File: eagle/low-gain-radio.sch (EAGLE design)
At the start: 118 parts, among them U1 MKW01Z128, U2 SKY65116, U3 W25Q80DV, U4 LP5907MFX-3.3, U5 NC7SZ05, U6 LP5907MFX-3.3, U7 LD39200, U8 MAAL-010704, U9 SKY13405-490LF, Y1 32MHz

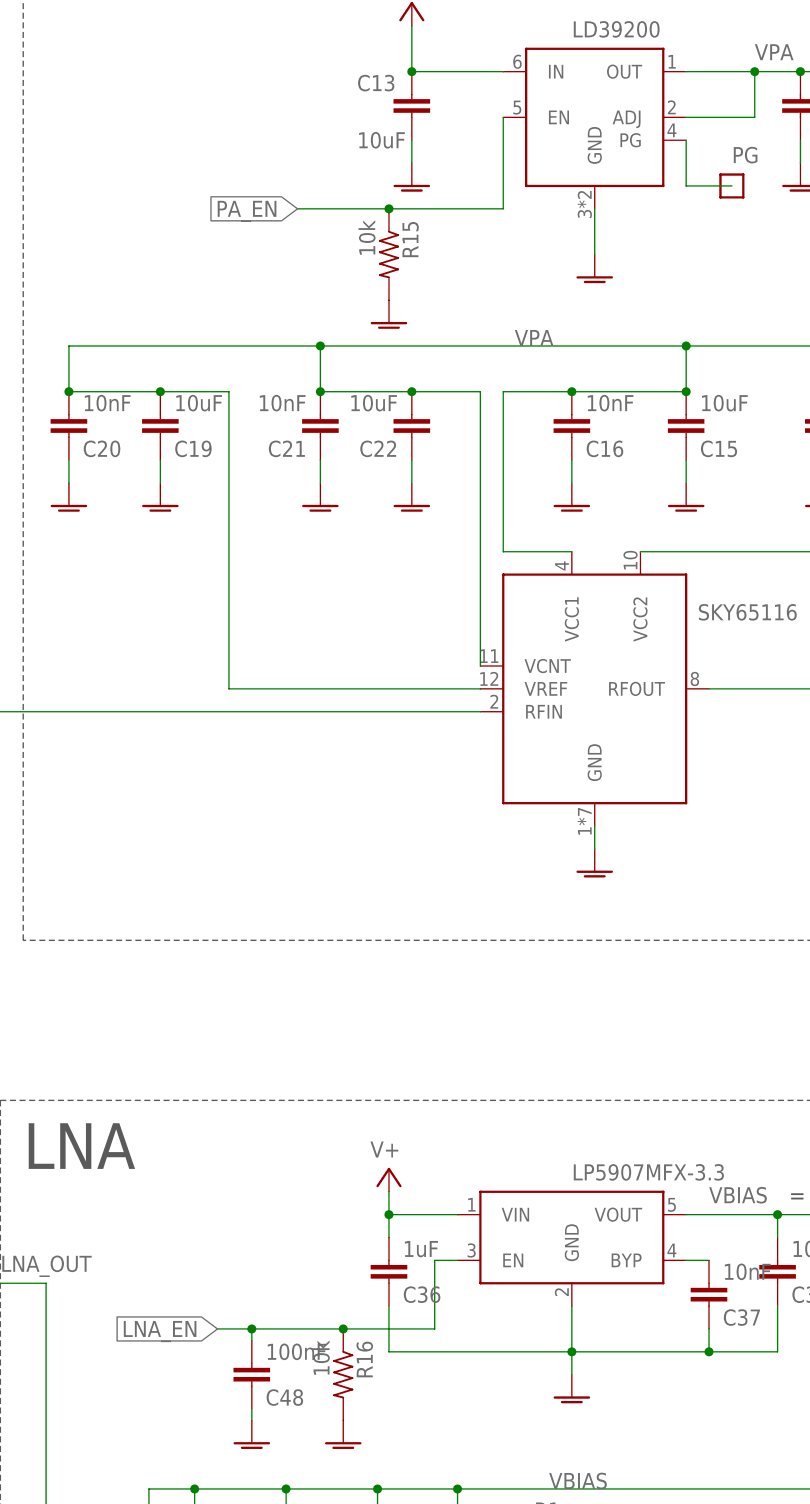
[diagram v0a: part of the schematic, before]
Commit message: Added test points for LNA and PA EN lines
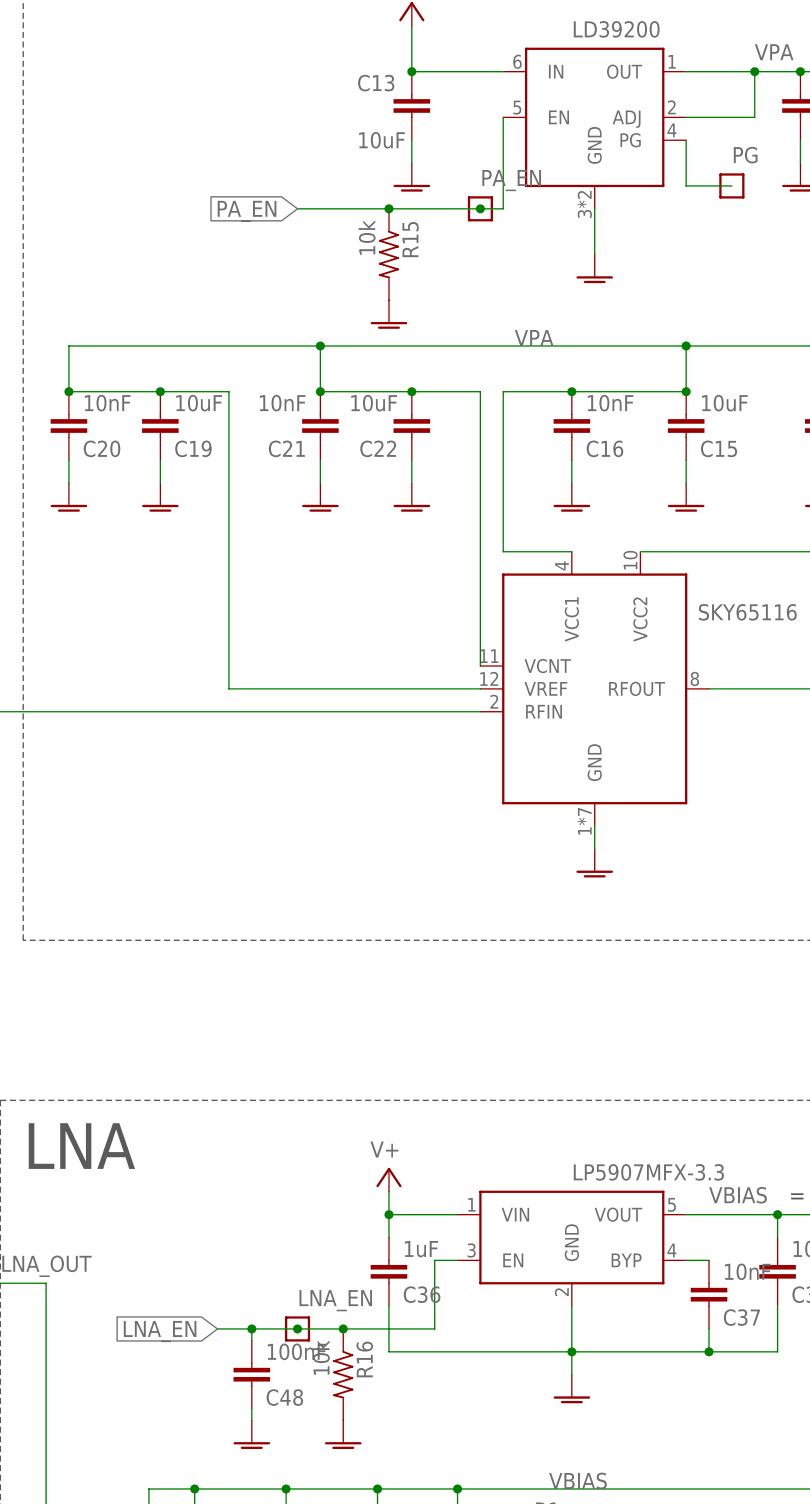
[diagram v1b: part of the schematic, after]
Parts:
- added LNA_EN, PA_EN: TEST-POINT, Tova:TEST-POINT
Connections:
- net LNA_EN: now also LNA_EN.1
- net PA_EN: now also PA_EN.1

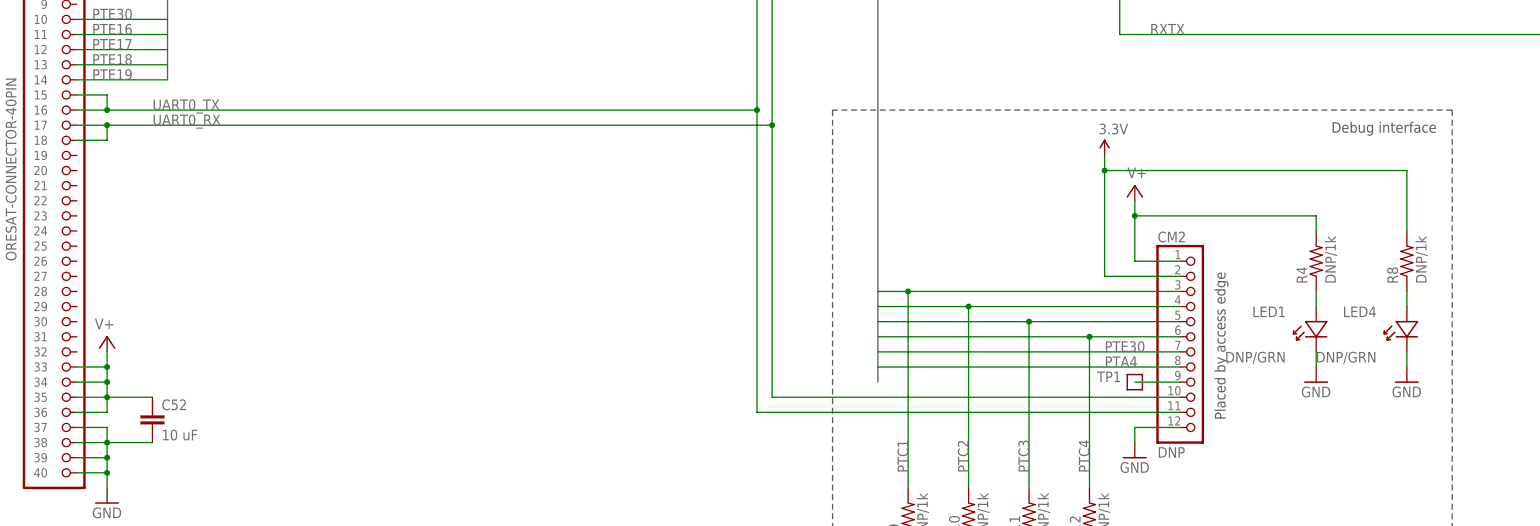
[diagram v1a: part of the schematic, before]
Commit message: Added LEDs for Rx and Tx
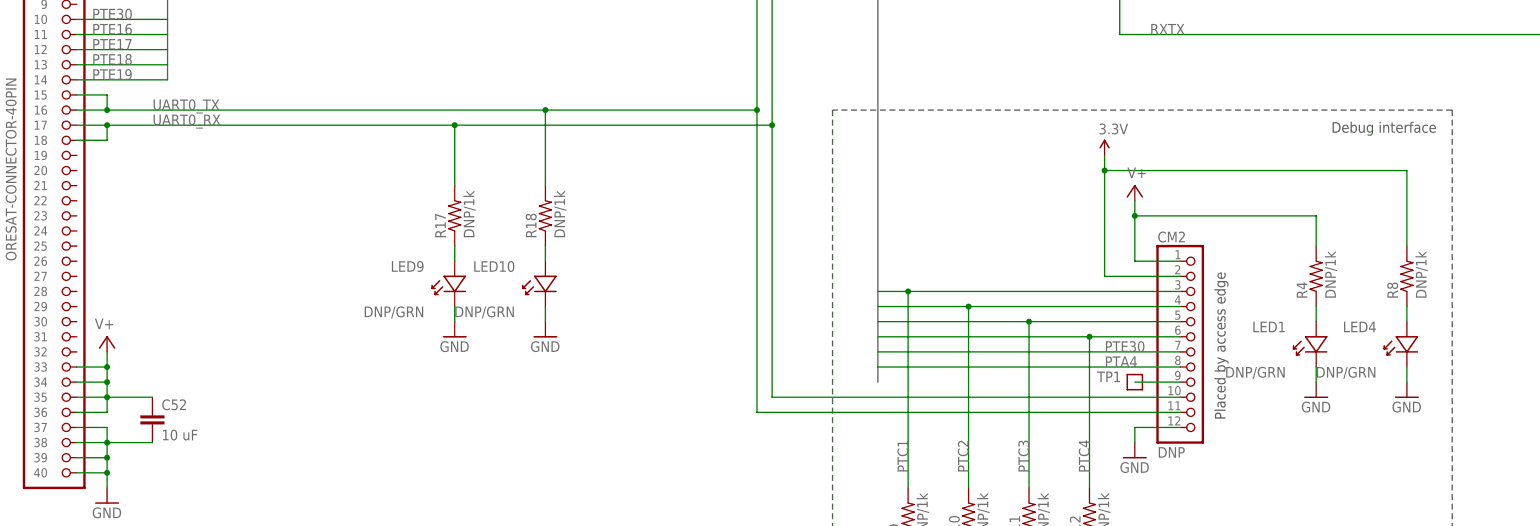
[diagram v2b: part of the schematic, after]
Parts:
- added LED10, LED9: DNP/GRN, psas_c3_team05:LED-0603
- added R17, R18: DNP/1k, rcl_custom:R-US_0603-B-NOSILK
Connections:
- new net N$6: LED9.A, R17.1
- new net N$9: LED10.A, R18.1
- net GND: now also LED10.K, LED9.K
- net UART0_RX: now also R17.2
- net UART0_TX: now also R18.2
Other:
- moved on the sheet: LED1, LED4, R4, R8

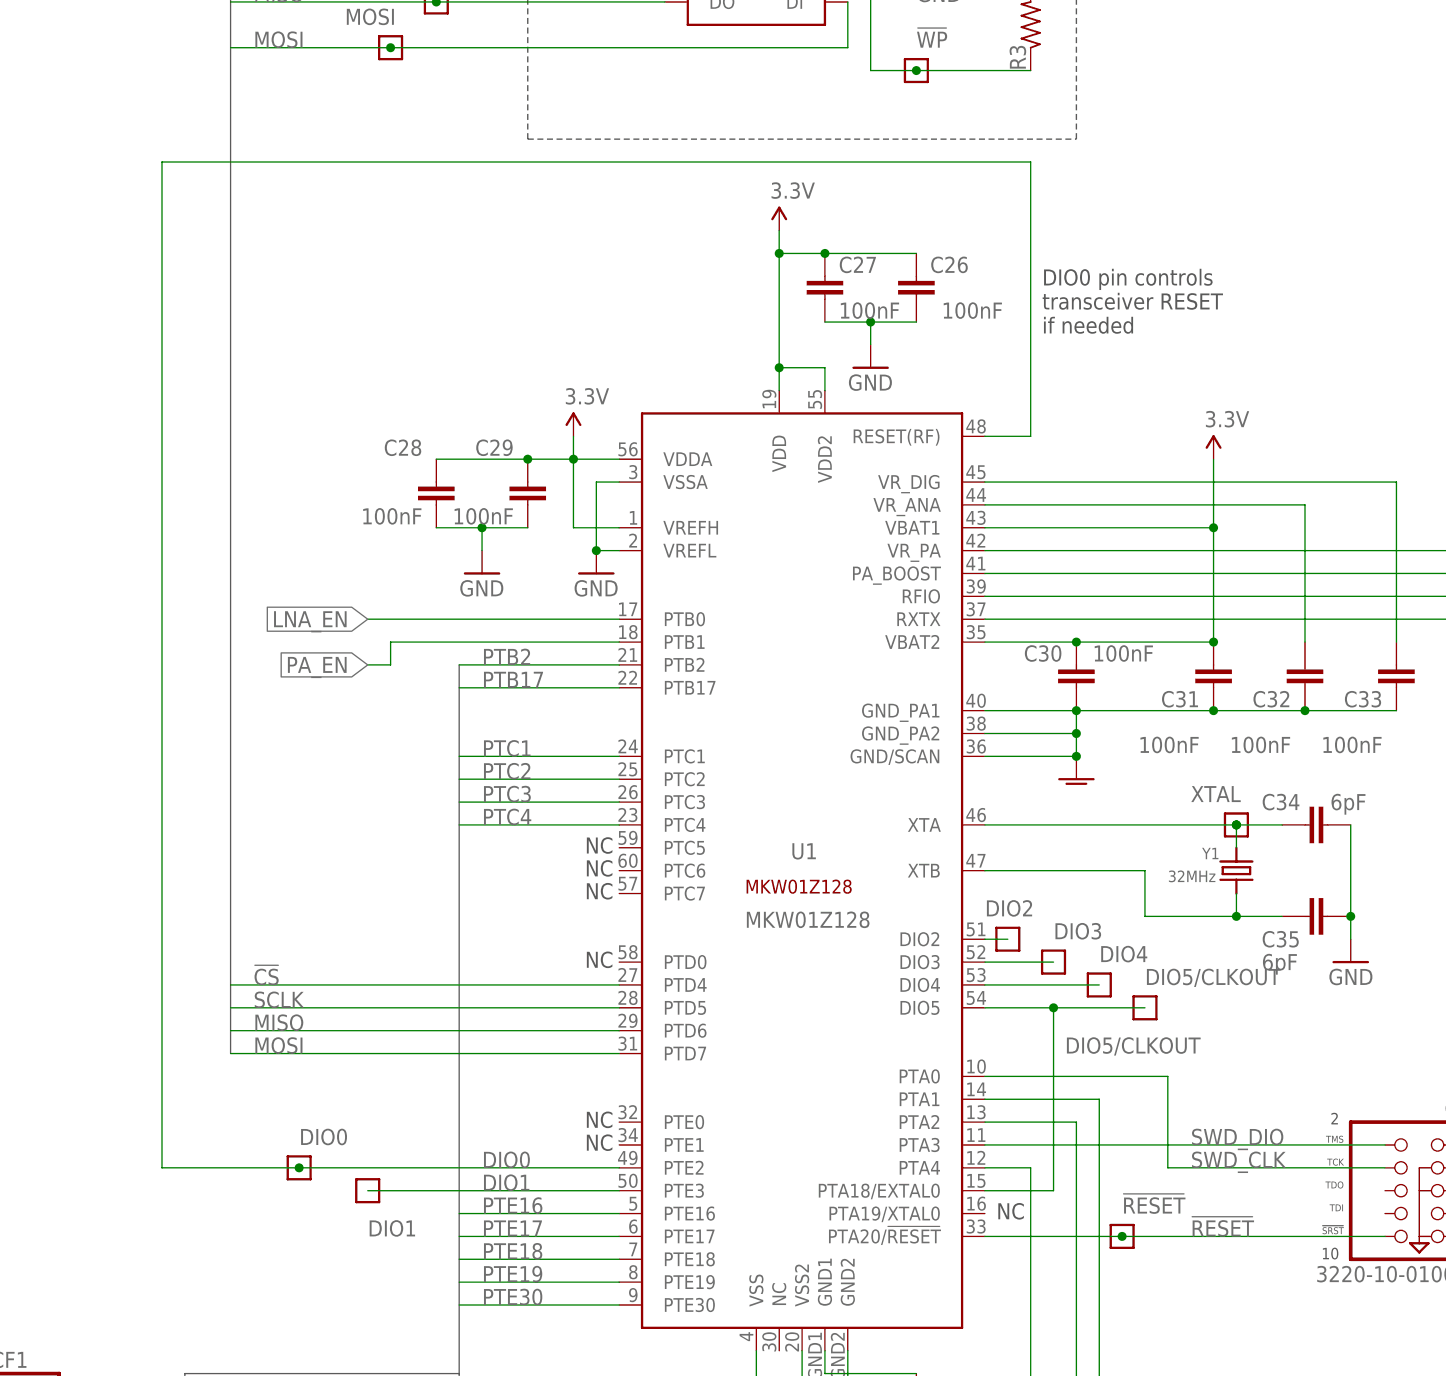
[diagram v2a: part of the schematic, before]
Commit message: Attached RESET(RF) to PTE16 instead of having it attached to DIO0
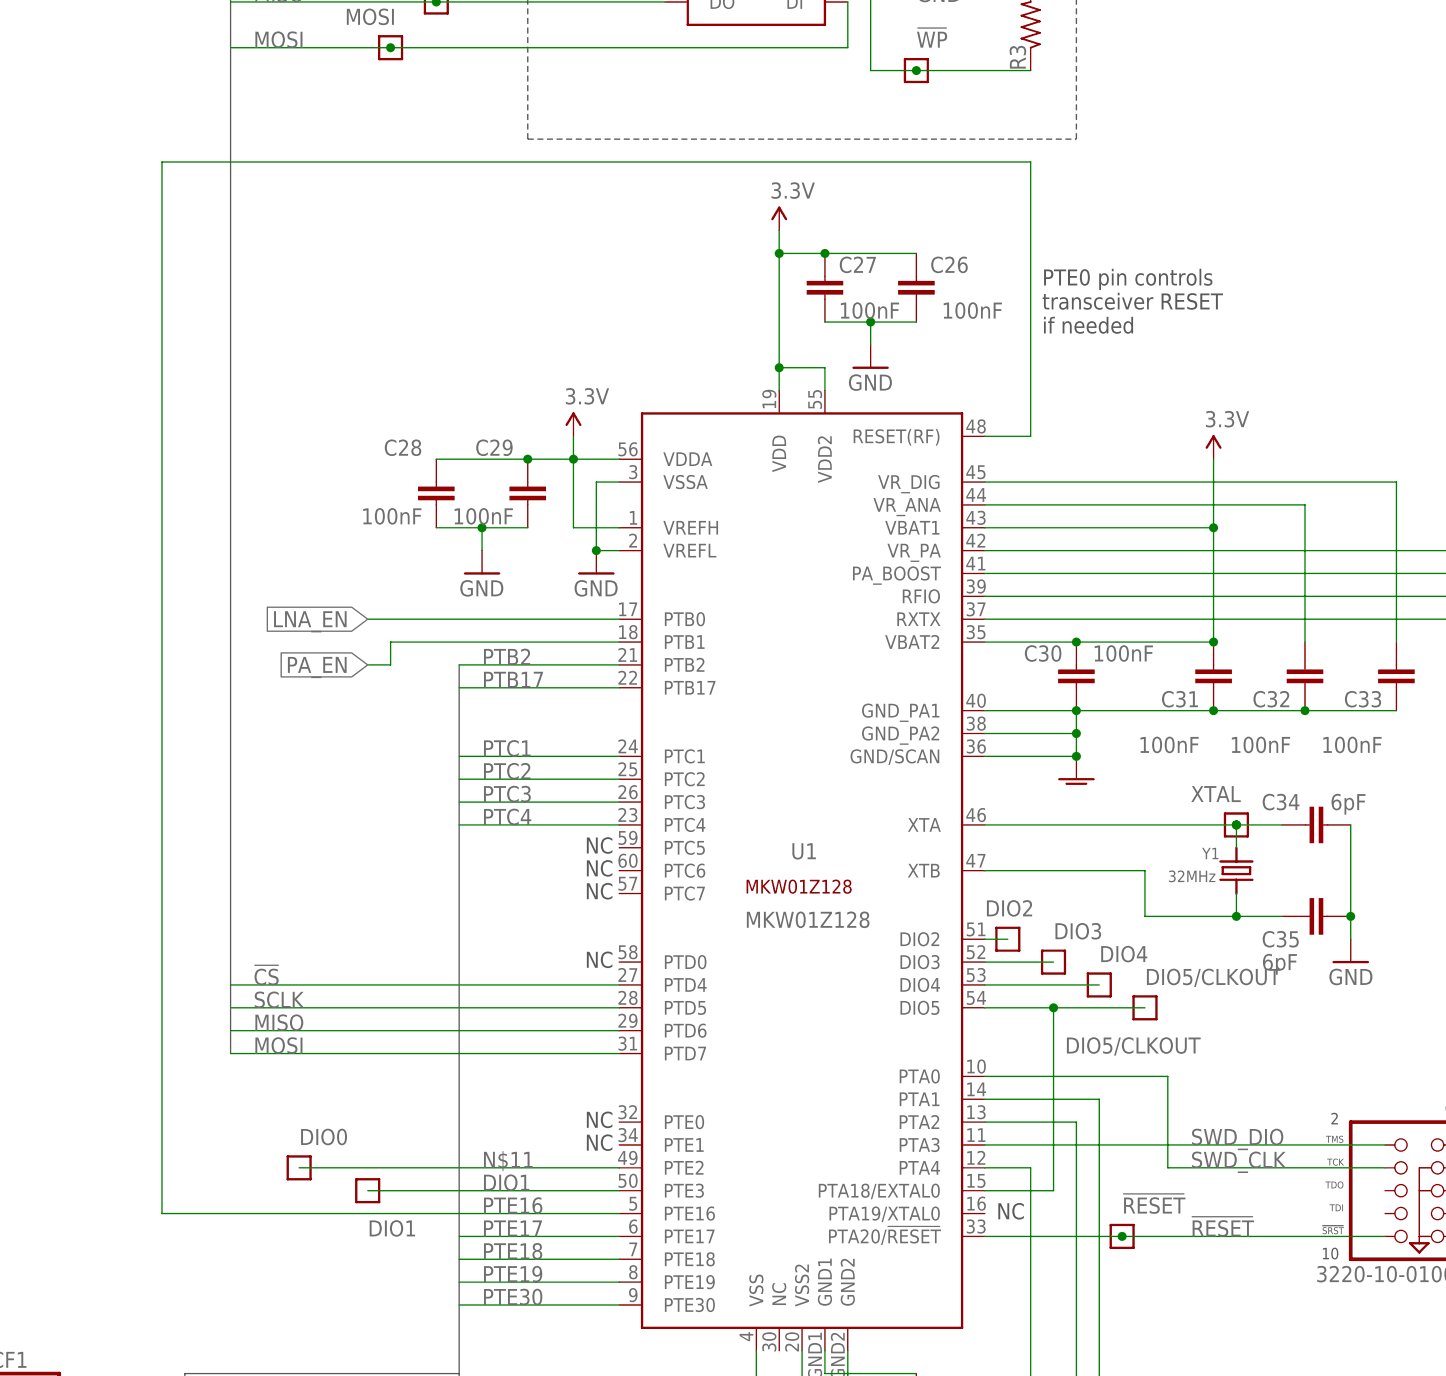
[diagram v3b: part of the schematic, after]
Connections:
- removed net DIO0: DIO0.1, U1.PTE2, U1.RESET(RF)
- new net N$11: DIO0.1, U1.PTE2
- net PTE16: now also U1.RESET(RF)
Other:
- note added: "PTE0 pin controls transceiver RESET if needed"
- note removed: "DIO0 pin controls transceiver RESET if needed"
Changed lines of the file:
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@@
 <setting verticaltext="up"/>
 </settings>
-<grid distance="0.05" unitdist="inch" unit="inch" style="lines" multiple="1" display="no" altdistance="0.01" altunitdist="inch" altunit="inch"/>
+<grid distance="0.1" unitdist="inch" unit="inch" style="lines" multiple="1" display="no" altdistance="0.01" altunitdist="inch" altunit="inch"/>
 <layers>
 <layer number="1" name="Top" color="4" fill="1" visible="no" active="no"/>
@@
 <text x="223.52" y="49.53" size="1.778" layer="97" rot="R90">Placed by access edge</text>
 <text x="7.62" y="154.94" size="1.778" layer="97" rot="R90">ORESAT BACKPLANE</text>
-<text x="140.97" y="257.81" size="1.778" layer="97">DIO0 pin controls
+<text x="140.97" y="257.81" size="1.778" layer="97">PTE0 pin controls
 transceiver RESET
 if needed</text>
@@
 <pinref part="CF1" gate="G$1" pin="11"/>
 </segment>
+<segment>
+<pinref part="U1" gate="G$1" pin="RESET(RF)"/>
+<wire x1="134.62" y1="246.38" x2="139.7" y2="246.38" width="0.1524" layer="91"/>
+<wire x1="139.7" y1="246.38" x2="139.7" y2="276.86" width="0.1524" layer="91"/>
+<wire x1="139.7" y1="276.86" x2="43.18" y2="276.86" width="0.1524" layer="91"/>
+<wire x1="43.18" y1="276.86" x2="43.18" y2="160.02" width="0.1524" layer="91"/>
+<wire x1="76.2" y1="160.02" x2="43.18" y2="160.02" width="0.1524" layer="91"/>
+</segment>
 </net>
 <net name="PTE17" class="0">
@@
 </segment>
 </net>
-<net name="DIO0" class="0">
-<segment>
-<pinref part="U1" gate="G$1" pin="RESET(RF)"/>
-<wire x1="134.62" y1="246.38" x2="139.7" y2="246.38" width="0.1524" layer="91"/>
-<wire x1="139.7" y1="246.38" x2="139.7" y2="276.86" width="0.1524" layer="91"/>
-<wire x1="139.7" y1="276.86" x2="43.18" y2="276.86" width="0.1524" layer="91"/>
-<wire x1="43.18" y1="276.86" x2="43.18" y2="165.1" width="0.1524" layer="91"/>
-<pinref part="U1" gate="G$1" pin="PTE2"/>
-<wire x1="93.98" y1="165.1" x2="58.42" y2="165.1" width="0.1524" layer="91"/>
-<label x="78.74" y="165.1" size="1.778" layer="95"/>
-<wire x1="43.18" y1="165.1" x2="58.42" y2="165.1" width="0.1524" layer="91"/>
-<pinref part="DIO0" gate="G$1" pin="1"/>
-<junction x="58.42" y="165.1"/>
-</segment>
-</net>
 <net name="DIO1" class="0">
 <segment>
@@
 </segment>
 </net>
+<net name="N$11" class="0">
+<segment>
+<pinref part="DIO0" gate="G$1" pin="1"/>
+<pinref part="U1" gate="G$1" pin="PTE2"/>
+<wire x1="93.98" y1="165.1" x2="58.42" y2="165.1" width="0.1524" layer="91"/>
+<label x="78.74" y="165.1" size="1.778" layer="95"/>
+</segment>
+</net>
